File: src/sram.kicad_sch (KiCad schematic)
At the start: 1 part, among them U10 IS61WV25616BLL-*BLI

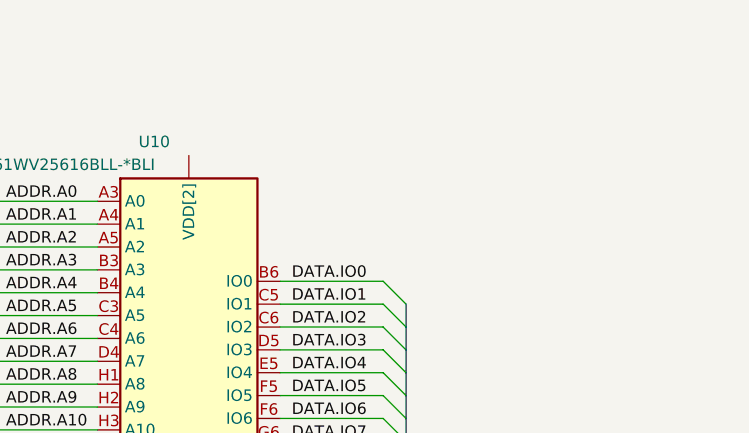
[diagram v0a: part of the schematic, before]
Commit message: Finishes the configuration schematic
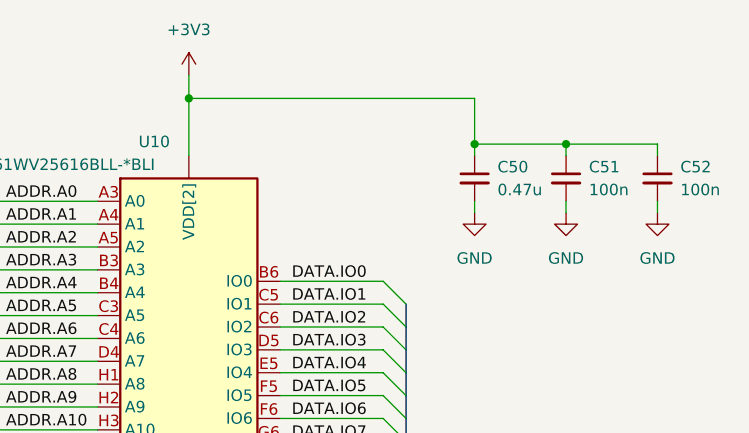
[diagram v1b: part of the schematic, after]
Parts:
- added C50: 0.47u, symbol Device:C_Small
- added C51, C52: 100n, symbol Device:C_Small
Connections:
- net GND: now also C50.2, C51.2, C52.2
- net VDD renamed +3V3
- net +3V3: now also C50.1, C51.1, C52.1

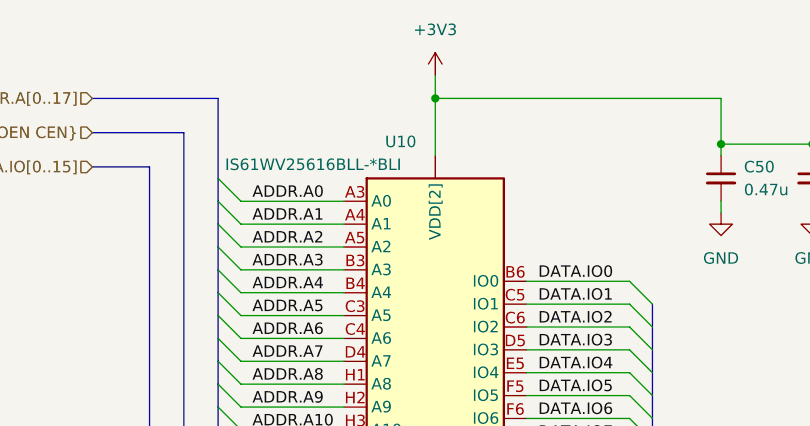
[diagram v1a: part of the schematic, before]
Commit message: Adds DDR symbol
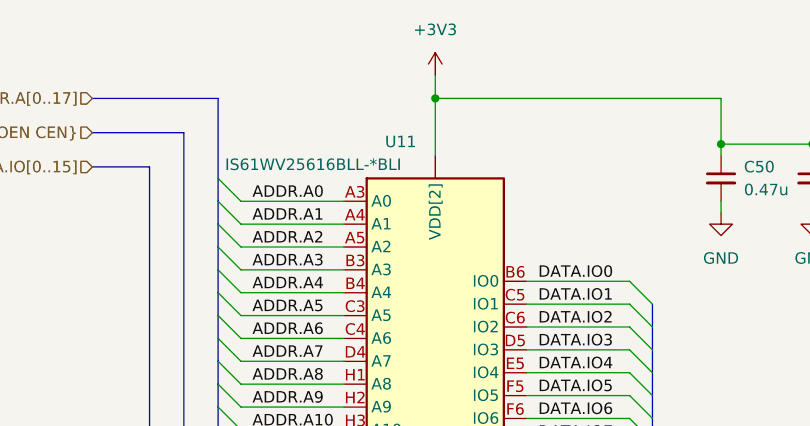
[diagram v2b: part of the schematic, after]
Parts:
- renumbered U10 to U11
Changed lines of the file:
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@@
 		(dnp no)
 		(fields_autoplaced yes)
-		(property "Reference" "#PWR049"
+		(property "Reference" "#PWR059"
 			(at 152.4 140.97 0)
 			(effects
@@
 		)
 		(instances
-			(project ""
-				(path "/c5fd18a3-9aa0-4151-b6e0-94da3d606686/492906df-f838-4d8b-b74b-2c5ce24fa298"
-					(reference "#PWR049")
+			(project "ecap5-bsom"
+				(path "/c5fd18a3-9aa0-4151-b6e0-94da3d606686/5eb51a9c-d950-4bb7-8ecf-1741d6933e12"
+					(reference "#PWR059")
 					(unit 1)
 				)
@@
 					(unit 1)
 				)
+				(path "/c5fd18a3-9aa0-4151-b6e0-94da3d606686/5eb51a9c-d950-4bb7-8ecf-1741d6933e12"
+					(reference "C53")
+					(unit 1)
+				)
 			)
 		)
@@
 					(unit 1)
 				)
+				(path "/c5fd18a3-9aa0-4151-b6e0-94da3d606686/5eb51a9c-d950-4bb7-8ecf-1741d6933e12"
+					(reference "C54")
+					(unit 1)
+				)
 			)
 		)
@@
 					(unit 1)
 				)
+				(path "/c5fd18a3-9aa0-4151-b6e0-94da3d606686/5eb51a9c-d950-4bb7-8ecf-1741d6933e12"
+					(reference "#PWR062")
+					(unit 1)
+				)
 			)
 		)
@@
 					(unit 1)
 				)
+				(path "/c5fd18a3-9aa0-4151-b6e0-94da3d606686/5eb51a9c-d950-4bb7-8ecf-1741d6933e12"
+					(reference "C55")
+					(unit 1)
+				)
 			)
 		)
@@
 		(dnp no)
 		(fields_autoplaced yes)
-		(property "Reference" "#PWR056"
+		(property "Reference" "#PWR058"
 			(at 152.4 57.15 0)
 			(effects
@@
 		)
 		(instances
-			(project ""
-				(path "/c5fd18a3-9aa0-4151-b6e0-94da3d606686/492906df-f838-4d8b-b74b-2c5ce24fa298"
-					(reference "#PWR056")
+			(project "ecap5-bsom"
+				(path "/c5fd18a3-9aa0-4151-b6e0-94da3d606686/5eb51a9c-d950-4bb7-8ecf-1741d6933e12"
+					(reference "#PWR058")
 					(unit 1)
 				)
@@
 		(on_board yes)
 		(dnp no)
-		(property "Reference" "U10"
+		(property "Reference" "U11"
 			(at 146.812 60.706 0)
 			(effects
@@
 		)
 		(instances
-			(project ""
-				(path "/c5fd18a3-9aa0-4151-b6e0-94da3d606686/492906df-f838-4d8b-b74b-2c5ce24fa298"
-					(reference "U10")
+			(project "ecap5-bsom"
+				(path "/c5fd18a3-9aa0-4151-b6e0-94da3d606686/5eb51a9c-d950-4bb7-8ecf-1741d6933e12"
+					(reference "U11")
 					(unit 1)
 				)
@@
 					(unit 1)
 				)
+				(path "/c5fd18a3-9aa0-4151-b6e0-94da3d606686/5eb51a9c-d950-4bb7-8ecf-1741d6933e12"
+					(reference "#PWR060")
+					(unit 1)
+				)
 			)
 		)
@@
 					(unit 1)
 				)
+				(path "/c5fd18a3-9aa0-4151-b6e0-94da3d606686/5eb51a9c-d950-4bb7-8ecf-1741d6933e12"
+					(reference "#PWR061")
+					(unit 1)
+				)

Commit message: Adds symbol for DDR2
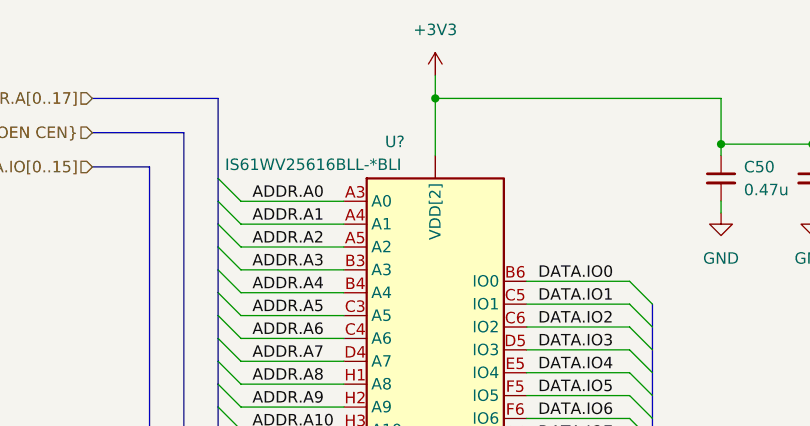
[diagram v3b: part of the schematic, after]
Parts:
- renumbered U11 to U?
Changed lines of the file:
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@@
 		(dnp no)
 		(fields_autoplaced yes)
-		(property "Reference" "#PWR059"
+		(property "Reference" "#PWR?"
 			(at 152.4 140.97 0)
 			(effects
@@
 		(instances
 			(project "ecap5-bsom"
-				(path "/c5fd18a3-9aa0-4151-b6e0-94da3d606686/5eb51a9c-d950-4bb7-8ecf-1741d6933e12"
-					(reference "#PWR059")
+				(path "/c5fd18a3-9aa0-4151-b6e0-94da3d606686/492906df-f838-4d8b-b74b-2c5ce24fa298"
+					(reference "#PWR?")
 					(unit 1)
 				)
@@
 					(unit 1)
 				)
-				(path "/c5fd18a3-9aa0-4151-b6e0-94da3d606686/5eb51a9c-d950-4bb7-8ecf-1741d6933e12"
-					(reference "C53")
-					(unit 1)
-				)
 			)
 		)
@@
 					(unit 1)
 				)
-				(path "/c5fd18a3-9aa0-4151-b6e0-94da3d606686/5eb51a9c-d950-4bb7-8ecf-1741d6933e12"
-					(reference "C54")
-					(unit 1)
-				)
 			)
 		)
@@
 					(unit 1)
 				)
-				(path "/c5fd18a3-9aa0-4151-b6e0-94da3d606686/5eb51a9c-d950-4bb7-8ecf-1741d6933e12"
-					(reference "#PWR062")
-					(unit 1)
-				)
 			)
 		)
@@
 					(unit 1)
 				)
-				(path "/c5fd18a3-9aa0-4151-b6e0-94da3d606686/5eb51a9c-d950-4bb7-8ecf-1741d6933e12"
-					(reference "C55")
-					(unit 1)
-				)
 			)
 		)
@@
 		(dnp no)
 		(fields_autoplaced yes)
-		(property "Reference" "#PWR058"
+		(property "Reference" "#PWR?"
 			(at 152.4 57.15 0)
 			(effects
@@
 		(instances
 			(project "ecap5-bsom"
-				(path "/c5fd18a3-9aa0-4151-b6e0-94da3d606686/5eb51a9c-d950-4bb7-8ecf-1741d6933e12"
-					(reference "#PWR058")
+				(path "/c5fd18a3-9aa0-4151-b6e0-94da3d606686/492906df-f838-4d8b-b74b-2c5ce24fa298"
+					(reference "#PWR?")
 					(unit 1)
 				)
@@
 		(on_board yes)
 		(dnp no)
-		(property "Reference" "U11"
+		(property "Reference" "U?"
 			(at 146.812 60.706 0)
 			(effects
@@
 		(instances
 			(project "ecap5-bsom"
-				(path "/c5fd18a3-9aa0-4151-b6e0-94da3d606686/5eb51a9c-d950-4bb7-8ecf-1741d6933e12"
-					(reference "U11")
+				(path "/c5fd18a3-9aa0-4151-b6e0-94da3d606686/492906df-f838-4d8b-b74b-2c5ce24fa298"
+					(reference "U?")
 					(unit 1)
 				)
@@
 					(unit 1)
 				)
-				(path "/c5fd18a3-9aa0-4151-b6e0-94da3d606686/5eb51a9c-d950-4bb7-8ecf-1741d6933e12"
-					(reference "#PWR060")
-					(unit 1)
-				)
 			)
 		)
@@
 					(unit 1)
 				)
-				(path "/c5fd18a3-9aa0-4151-b6e0-94da3d606686/5eb51a9c-d950-4bb7-8ecf-1741d6933e12"
-					(reference "#PWR061")
-					(unit 1)
-				)

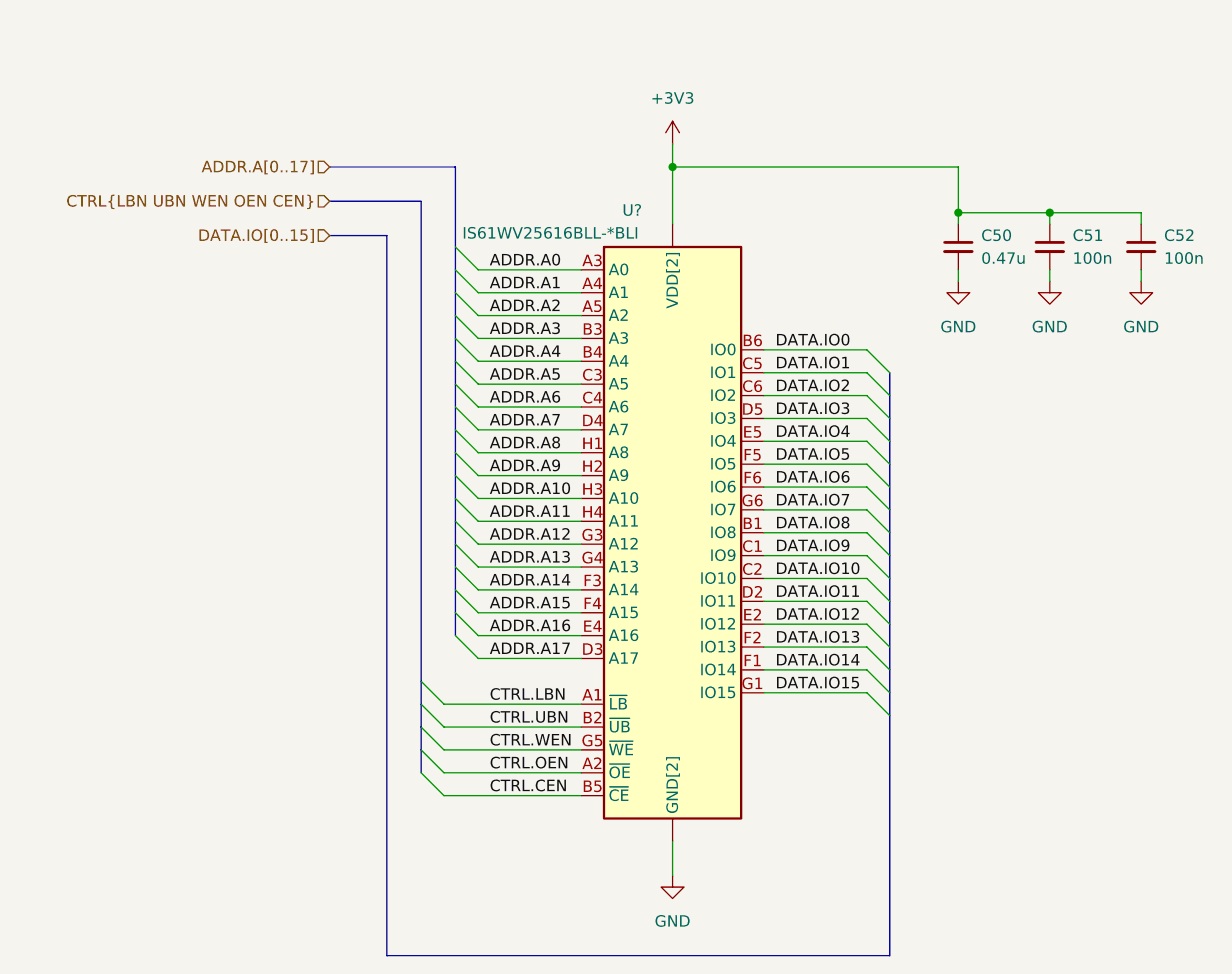
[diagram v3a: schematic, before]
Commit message: Adds DDR2 schematic
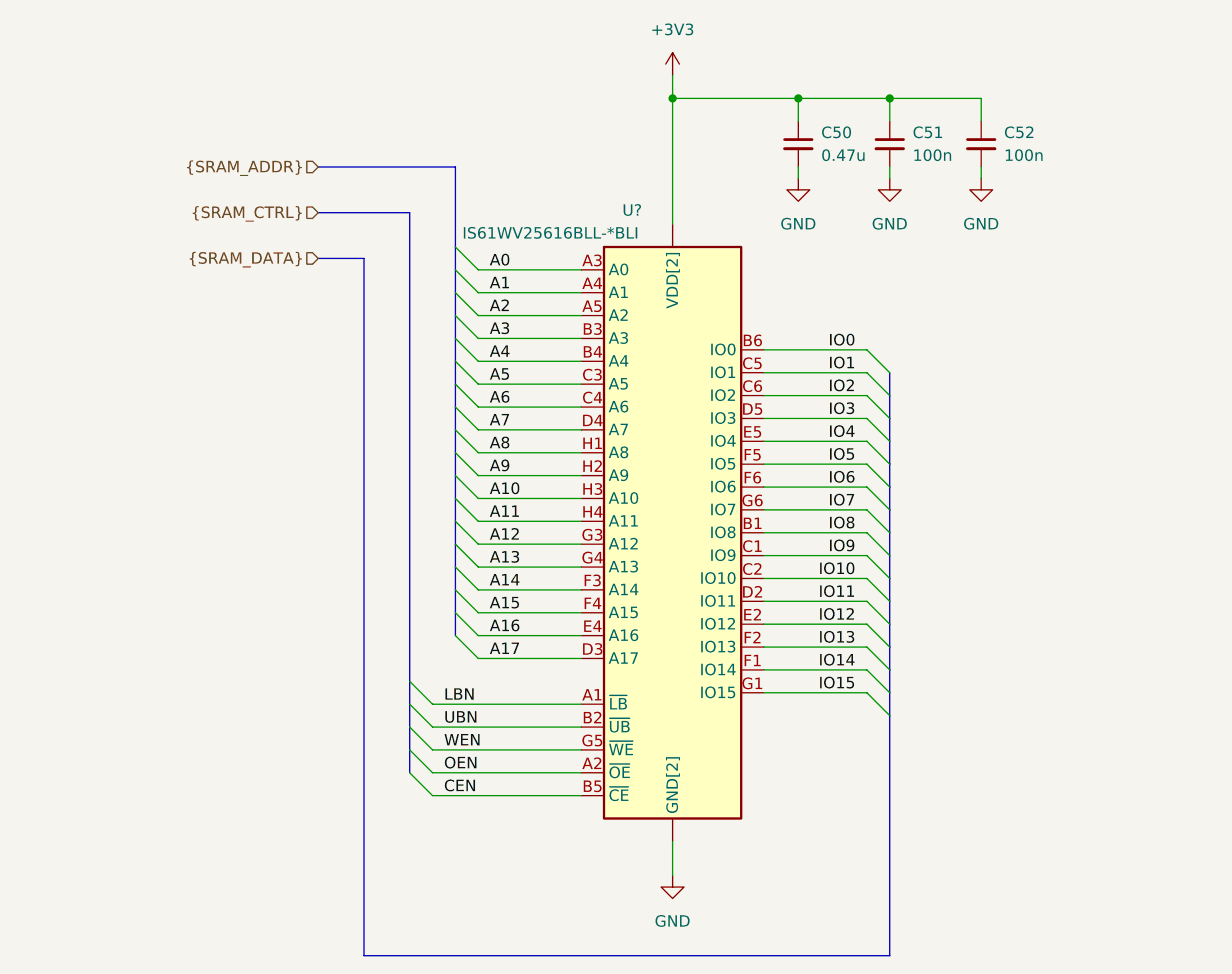
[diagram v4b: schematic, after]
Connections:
- net ADDR.A8 is gone; now on net NC: U?.H1 (NC)
- net ADDR.A0 renamed A0
- net ADDR.A1 renamed A1
- net ADDR.A10 renamed A10
- net ADDR.A11 renamed A11
- net ADDR.A12 renamed A12
- net ADDR.A13 renamed A13
- net ADDR.A14 renamed A14
- net ADDR.A15 renamed A15
- net ADDR.A16 renamed A16
- net ADDR.A17 renamed A17
- net ADDR.A2 renamed A2
- net ADDR.A3 renamed A3
- net ADDR.A4 renamed A4
- net ADDR.A5 renamed A5
- net ADDR.A6 renamed A6
- net ADDR.A7 renamed A7
- net ADDR.A9 renamed A9
- net CTRL.CEN renamed CEN
- net CTRL.LBN renamed LBN
- net CTRL.OEN renamed OEN
- net CTRL.UBN renamed UBN
- net CTRL.WEN renamed WEN
- net DATA.IO0 renamed IO0
- net DATA.IO1 renamed IO1
- net DATA.IO10 renamed IO10
- net DATA.IO11 renamed IO11
- net DATA.IO12 renamed IO12
- net DATA.IO13 renamed IO13
- net DATA.IO14 renamed IO14
- net DATA.IO15 renamed IO15
- net DATA.IO2 renamed IO2
- net DATA.IO3 renamed IO3
- net DATA.IO4 renamed IO4
- net DATA.IO5 renamed IO5
- net DATA.IO6 renamed IO6
- net DATA.IO7 renamed IO7
- net DATA.IO8 renamed IO8
- net DATA.IO9 renamed IO9
- new net A8: U?.H1 (NC)
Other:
- moved on the sheet: C50, C51, C52

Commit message: Finishes the ram schematic
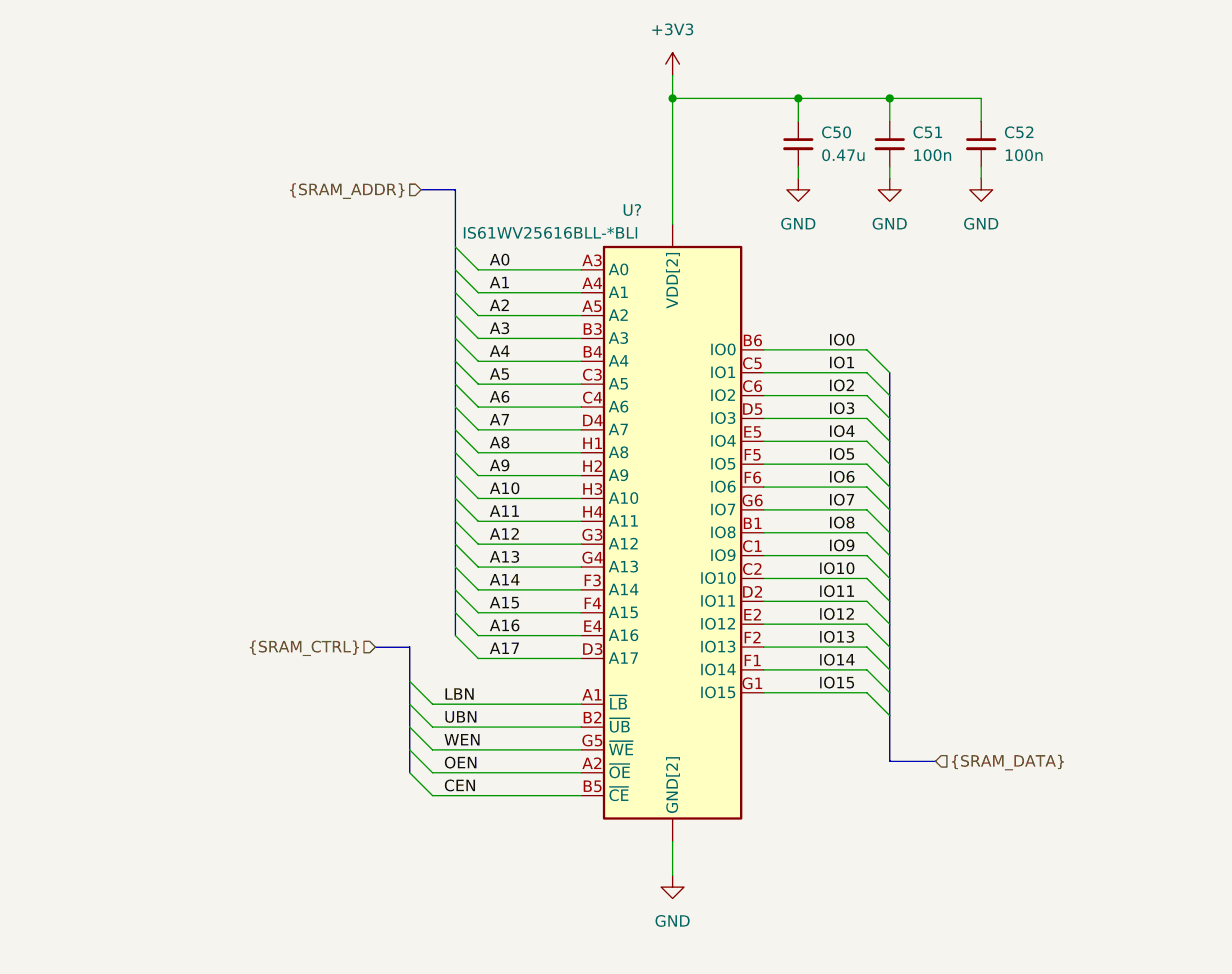
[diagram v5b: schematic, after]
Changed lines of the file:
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@@
-		)
-	)
-	(bus
-		(pts
-			(xy 118.11 66.04) (xy 118.11 143.51)
-		)
-		(stroke
-			(width 0)
-			(type default)
 		)
 	)
@@
 	(bus
 		(pts
-			(xy 123.19 60.96) (xy 123.19 113.03)
+			(xy 123.19 109.22) (xy 123.19 113.03)
 		)
 		(stroke
@@
 		)
 	)
-	(bus
-		(pts
-			(xy 118.11 143.51) (xy 176.53 143.51)
-		)
-		(stroke
-			(width 0)
-			(type default)
-		)
-	)
 	(wire
 		(pts
@@
 	(bus
 		(pts
-			(xy 176.53 143.51) (xy 176.53 116.84)
-		)
-		(stroke
-			(width 0)
-			(type default)
-		)
-	)
-	(bus
-		(pts
-			(xy 113.03 55.88) (xy 128.27 55.88)
+			(xy 124.46 58.42) (xy 128.27 58.42)
 		)
 		(stroke
@@
 	(bus
 		(pts
-			(xy 128.27 55.88) (xy 128.27 64.77)
+			(xy 128.27 58.42) (xy 128.27 64.77)
 		)
 		(stroke
@@
 		)
 	)
-	(bus
-		(pts
-			(xy 113.03 66.04) (xy 118.11 66.04)
-		)
-		(stroke
-			(width 0)
-			(type default)
-		)
-	)
 	(wire
 		(pts
@@
 	(bus
 		(pts
-			(xy 113.03 60.96) (xy 123.19 60.96)
+			(xy 176.53 121.92) (xy 176.53 116.84)
+		)
+		(stroke
+			(width 0)
+			(type default)
+		)
+	)
+	(bus
+		(pts
+			(xy 119.38 109.22) (xy 123.19 109.22)
 		)
 		(stroke
@@
 		(pts
 			(xy 130.81 90.17) (xy 142.24 90.17)
+		)
+		(stroke
+			(width 0)
+			(type default)
+		)
+	)
+	(bus
+		(pts
+			(xy 176.53 121.92) (xy 181.61 121.92)
 		)
 		(stroke
@@
 	(hierarchical_label "{SRAM_ADDR}"
 		(shape input)
-		(at 113.03 55.88 180)
+		(at 124.46 58.42 180)
 		(fields_autoplaced yes)
 		(effects
@@
 	(hierarchical_label "{SRAM_DATA}"
 		(shape input)
-		(at 113.03 66.04 180)
-		(fields_autoplaced yes)
-		(effects
-			(font
-				(size 1.27 1.27)
-			)
-			(justify right)
+		(at 181.61 121.92 0)
+		(fields_autoplaced yes)
+		(effects
+			(font
+				(size 1.27 1.27)
+			)
+			(justify left)
 		)
 	)
 	(hierarchical_label "{SRAM_CTRL}"
 		(shape input)
-		(at 113.03 60.96 180)
-		(fields_autoplaced yes)
-		(effects
+		(at 119.38 109.22 180)
+		(fields_autoplaced yes)
+		(effects

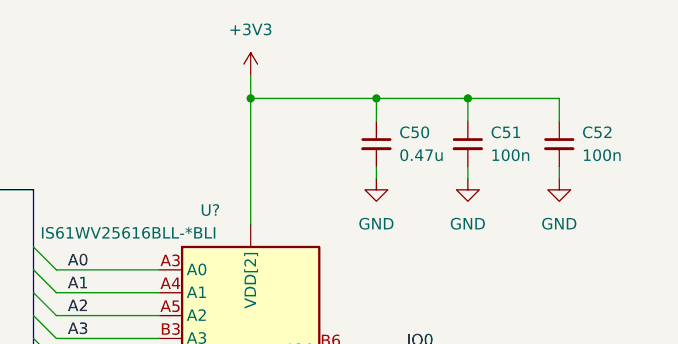
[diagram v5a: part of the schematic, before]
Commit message: Add the eMMC
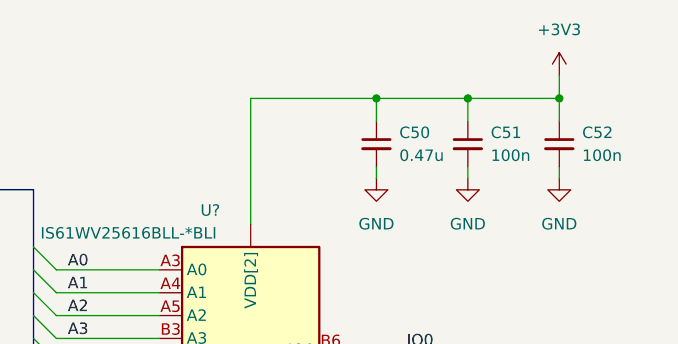
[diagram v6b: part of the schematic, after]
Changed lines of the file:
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@@
+	)
+	(junction
+		(at 186.69 48.26)
+		(diameter 0)
+		(color 0 0 0 0)
 	)
 	(junction
@@
 		(color 0 0 0 0)
 	)
-	(junction
-		(at 152.4 48.26)
-		(diameter 0)
-		(color 0 0 0 0)
-	)
 	(bus_entry
 		(at 128.27 100.33)
@@
 		)
 	)
+	(wire
+		(pts
+			(xy 176.53 48.26) (xy 166.37 48.26)
+		)
+		(stroke
+			(width 0)
+			(type default)
+		)
+	)
 	(bus
 		(pts
@@
 		)
 	)
-	(wire
-		(pts
-			(xy 166.37 48.26) (xy 176.53 48.26)
-		)
-		(stroke
-			(width 0)
-			(type default)
-		)
-	)
 	(bus
 		(pts
@@
 	(wire
 		(pts
-			(xy 152.4 45.72) (xy 152.4 48.26)
+			(xy 186.69 45.72) (xy 186.69 48.26)
 		)
 		(stroke
@@
 	(symbol
 		(lib_id "power:+3V3")
-		(at 152.4 45.72 0)
+		(at 186.69 45.72 0)
 		(unit 1)
 		(exclude_from_sim no)
@@
 		(fields_autoplaced yes)
 		(property "Reference" "#PWR?"
-			(at 152.4 49.53 0)
+			(at 186.69 49.53 0)
 			(effects
 				(font
@@
 		)
 		(property "Value" "+3V3"
-			(at 152.4 40.64 0)
+			(at 186.69 40.64 0)
 			(effects
 				(font
@@
 		)
 		(property "Footprint" ""
-			(at 152.4 45.72 0)
+			(at 186.69 45.72 0)
 			(effects
 				(font
@@
 		)
 		(property "Datasheet" ""
-			(at 152.4 45.72 0)
+			(at 186.69 45.72 0)
 			(effects
 				(font
@@
 		)
 		(property "Description" "Power symbol creates a global label with name \"+3V3\""
-			(at 152.4 45.72 0)
-			(effects
-				(font
+			(at 186.69 45.72 0)
+			(effects
+				(font
